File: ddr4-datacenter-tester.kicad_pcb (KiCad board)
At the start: 8 copper layers, 152.9 x 90 mm, 377 parts, among them IC1 TPS54561, IC3 TPD8S009DSMR, J1 0878311420, J10 61300311121, J3 DC_SOCKET, J4 WE_629105150521, J5 2309409-1, J6 685119134923, J7 1140084168, J8 61300311121, Q2 BSS138APW, Q3 BSS138APW, Q4 BSS138APW, Q5 BSS138APW, Q6 BSS138APW, Q7 BSS138APW, Q8 BSS138APW, U1 XC7K70T-FBG484, U10 LM3881MME_NOPB, U11 S27KL0641DABHI023, U12 TPS62823DLCT, U13 XC7K160T-2FFG676C, U14 2199155-1, U2 ASFLMB-100.000MHZ-XY-T, U3 S25FL128SAGNFI000, U4 TPS65296, U5 TPS62823DLCT, U6 KSZ9031RNXCA, U7 FT4232HQ, U8 SRST, U9 TPS62823DLCT, Y1 ABM8G-25.000MHZ-18-D2Y-T, Y2 ABM8G-12.000MHZ-18-D2Y-T

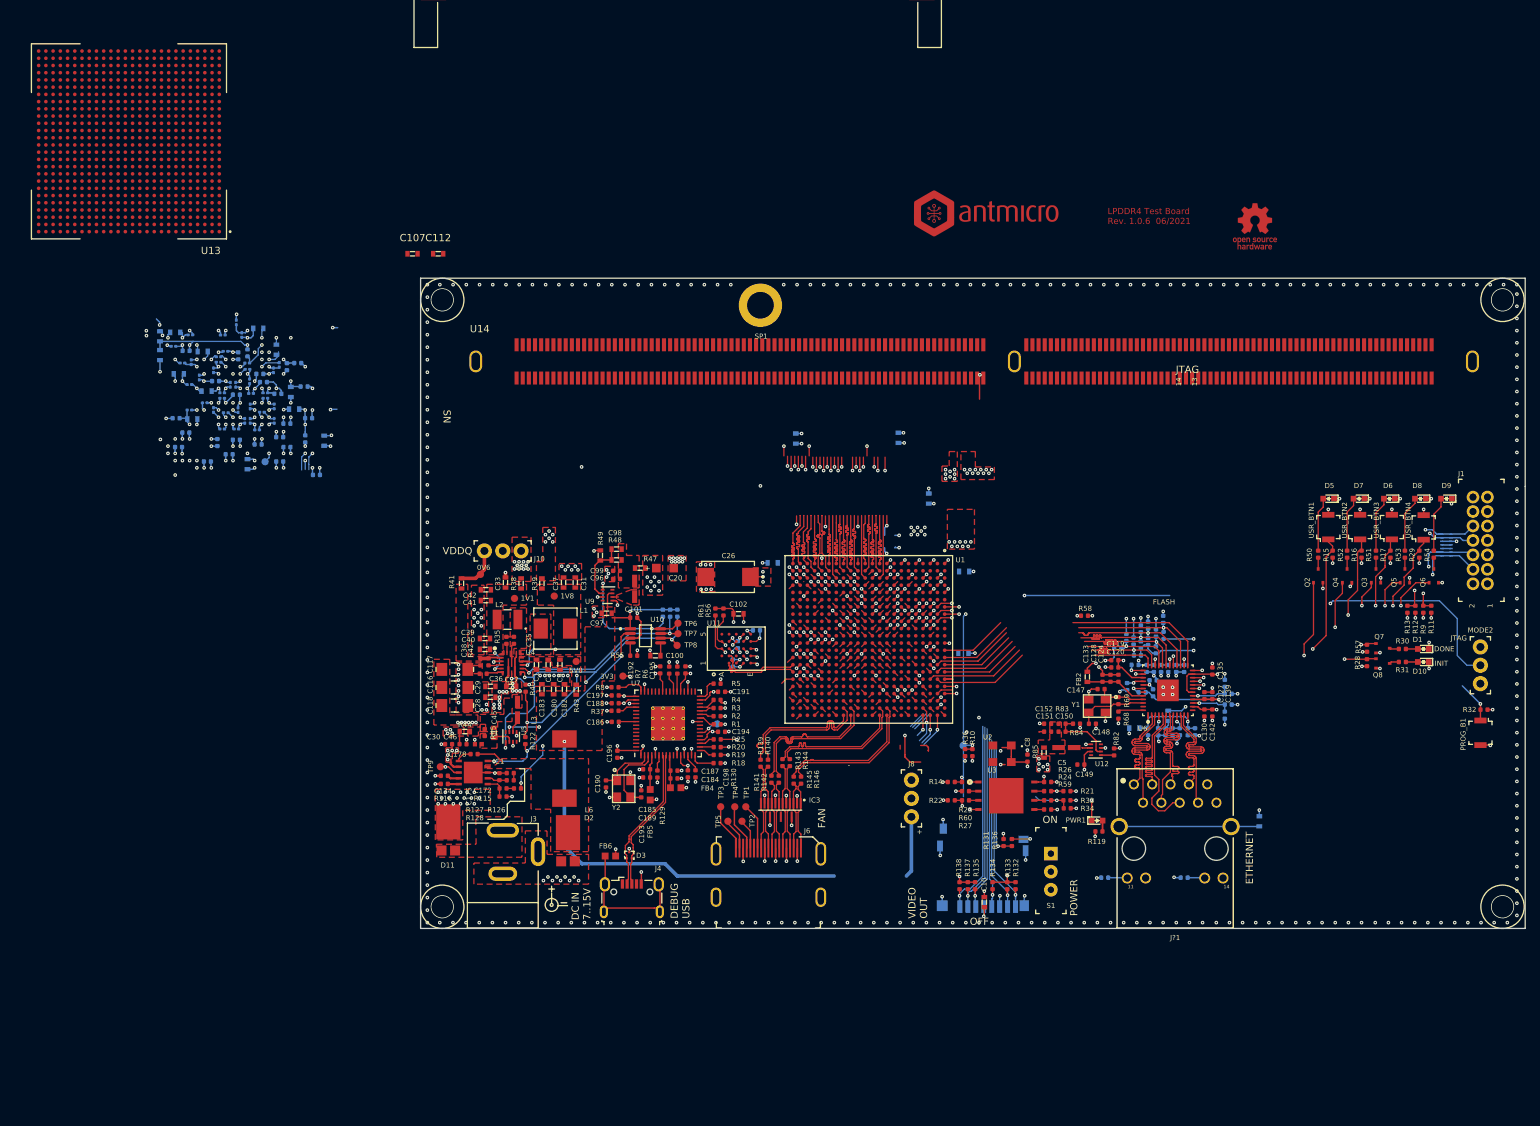
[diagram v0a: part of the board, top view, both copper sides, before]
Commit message: Component placement draft
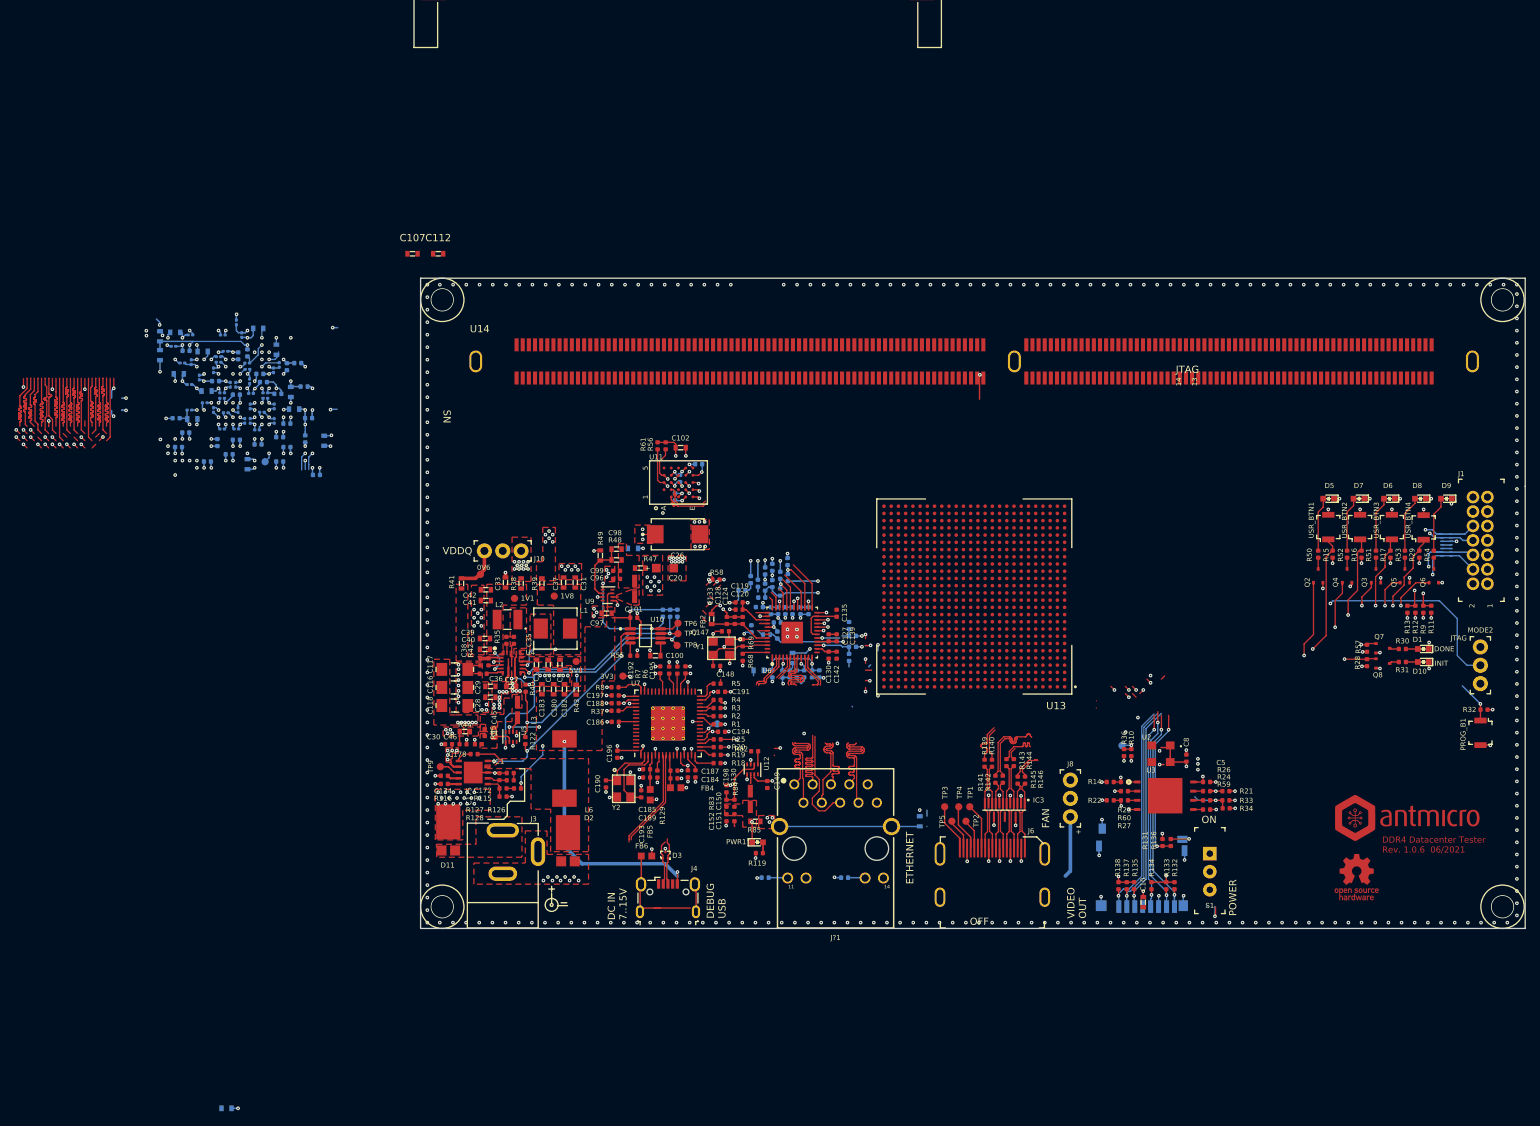
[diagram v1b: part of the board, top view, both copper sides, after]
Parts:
- removed C106, C108, C110, C111: C_10n_0603, ddr4-datacenter-tester-footprints:0603-cap
- removed SP1: 9774050151, ddr4-datacenter-tester-footprints:9774050151
- removed U1: XC7K70T-FBG484, ddr4-datacenter-tester-footprints:BGA484C100P22X22_2300X2300X244N
- moved U13 132.9 mm to (183.6, 90.1)
- moved C113 119.9 mm to (80.1, 160.9)
- moved N2 102.0 mm to (243.6, 120.9)
- moved N1 91.2 mm to (236.6, 128.9)
- moved C119 52.6 mm to (151.1, 90.9)
- moved C120 52.6 mm to (151.1, 91.9)
- moved C121 52.6 mm to (157.1, 100.8)
- moved C122 52.6 mm to (157.5, 92.0)
- moved C123 52.6 mm to (155.5, 92.0)
- moved C124 52.6 mm to (151.6, 93.4)
- moved C125 52.6 mm to (160.1, 100.8)
- moved C126 52.6 mm to (159.6, 92.0)
- moved C127 52.6 mm to (163.5, 95.8)
- moved C128 52.6 mm to (150.5, 93.4)
- moved C129 52.6 mm to (158.1, 100.8)
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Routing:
- net GND: track 317.8 -> 237.5 mm, vias 516 -> 465
- net TCK_JTAG: track 97.1 -> 31.1 mm
- net TDO_JTAG: track 94.5 -> 29.6 mm
- net TDI_JTAG: track 96.3 -> 31.9 mm
- net TMS_JTAG: track 91.1 -> 26.8 mm
- net /Supply/SYS_EN: track 85.0 -> 22.4 mm, vias 1 -> 0
- net /Supply/VCC_IO_EN: track 137.1 -> 84.7 mm, vias 5 -> 4
- net PROGRAM_B: track 53.2 -> 5.91 mm, vias 3 -> 1
- net DONE: track 41.4 -> 5.33 mm, vias 2 -> 1
- net CCLK: track 41.1 -> 5.95 mm, vias 3 -> 1
- net INIT_B: track 35.1 -> 5.05 mm, vias 2 -> 1
- net 3V3_SYS: track 156.3 -> 126.3 mm, vias 87 -> 86
- net MODE0: track 42.3 -> 13.0 mm, vias 2 -> 1
- net MODE1: track 41.2 -> 12.0 mm, vias 2 -> 1
- net ETH_RXD0: track 32.2 -> 5.04 mm
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- removed copper zone on F.Cu, net VDDQ
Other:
- board text added: "DDR4 Datacenter Tester Rev. 1.0.0 06/2021"
- board text added: "DDR4 Datacenter Tester Rev. 1.0.6 06/2021"
- board text removed: "-"
- board text removed: "FLASH"
- board text removed: "LPDDR4 Test Board Rev. 1.0.6 06/2021"

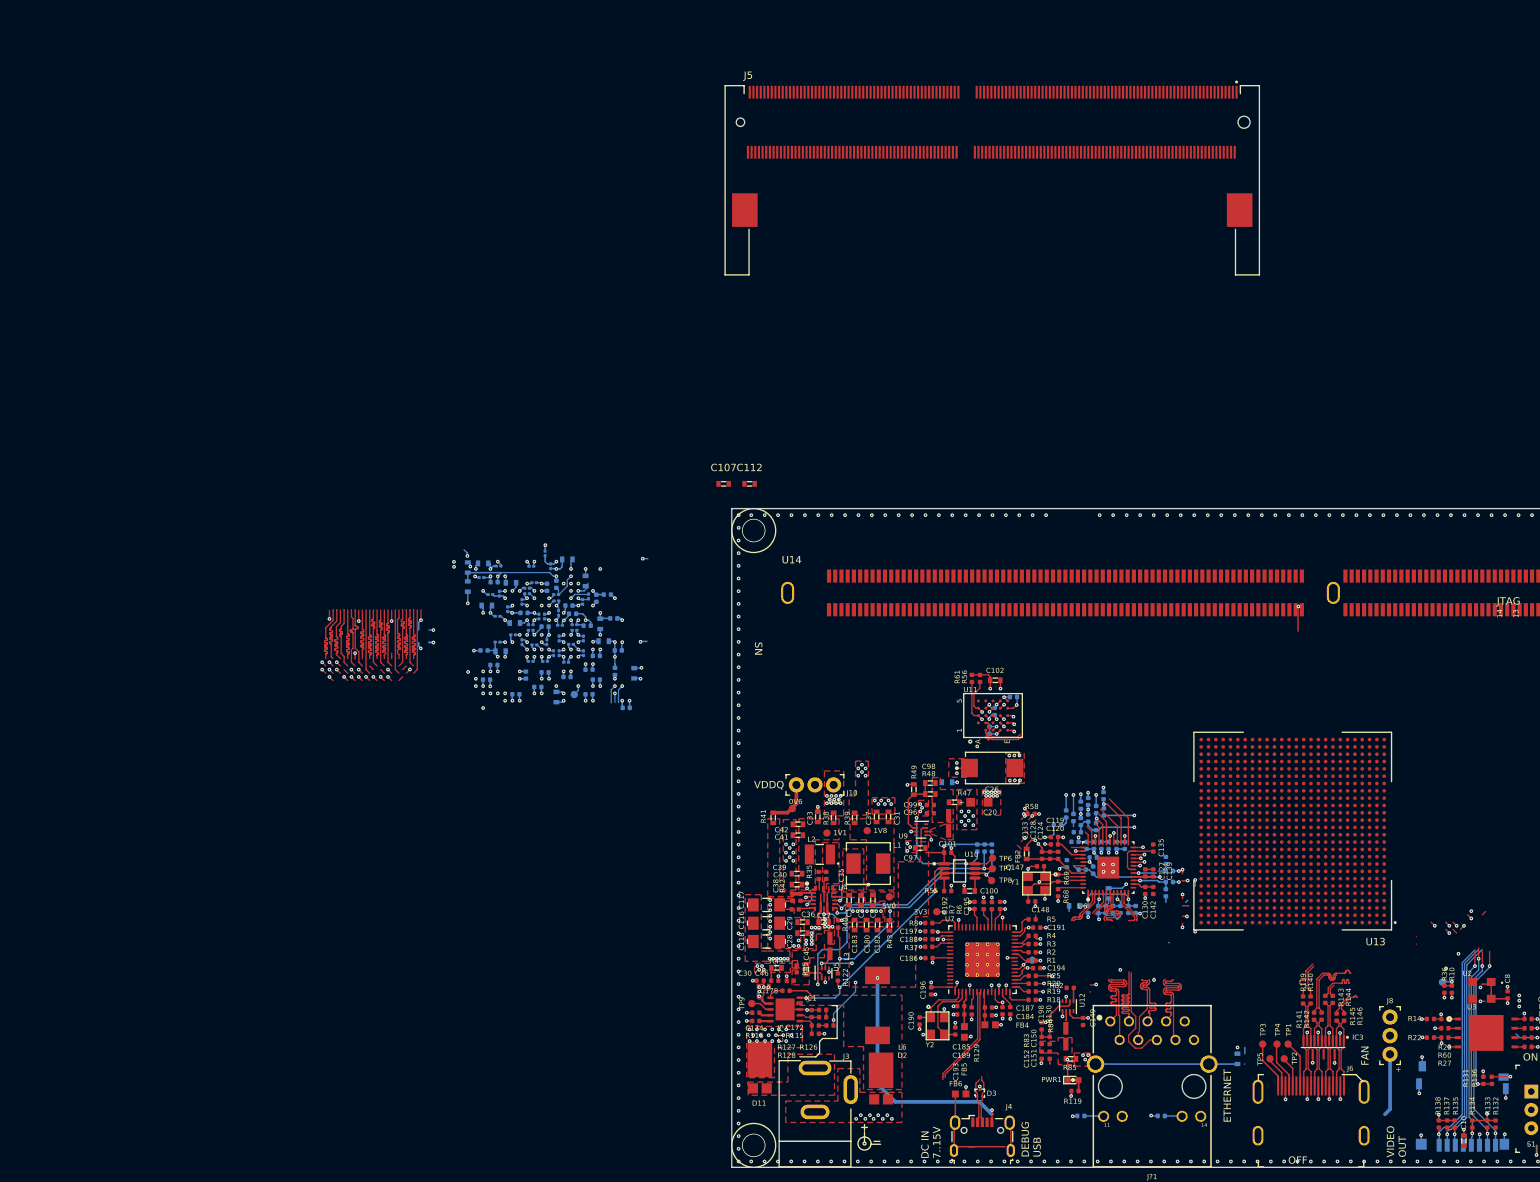
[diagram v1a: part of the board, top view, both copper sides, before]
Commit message: Add DD4 pinout, connect ethernet, QSPI, TMDS, SDIO
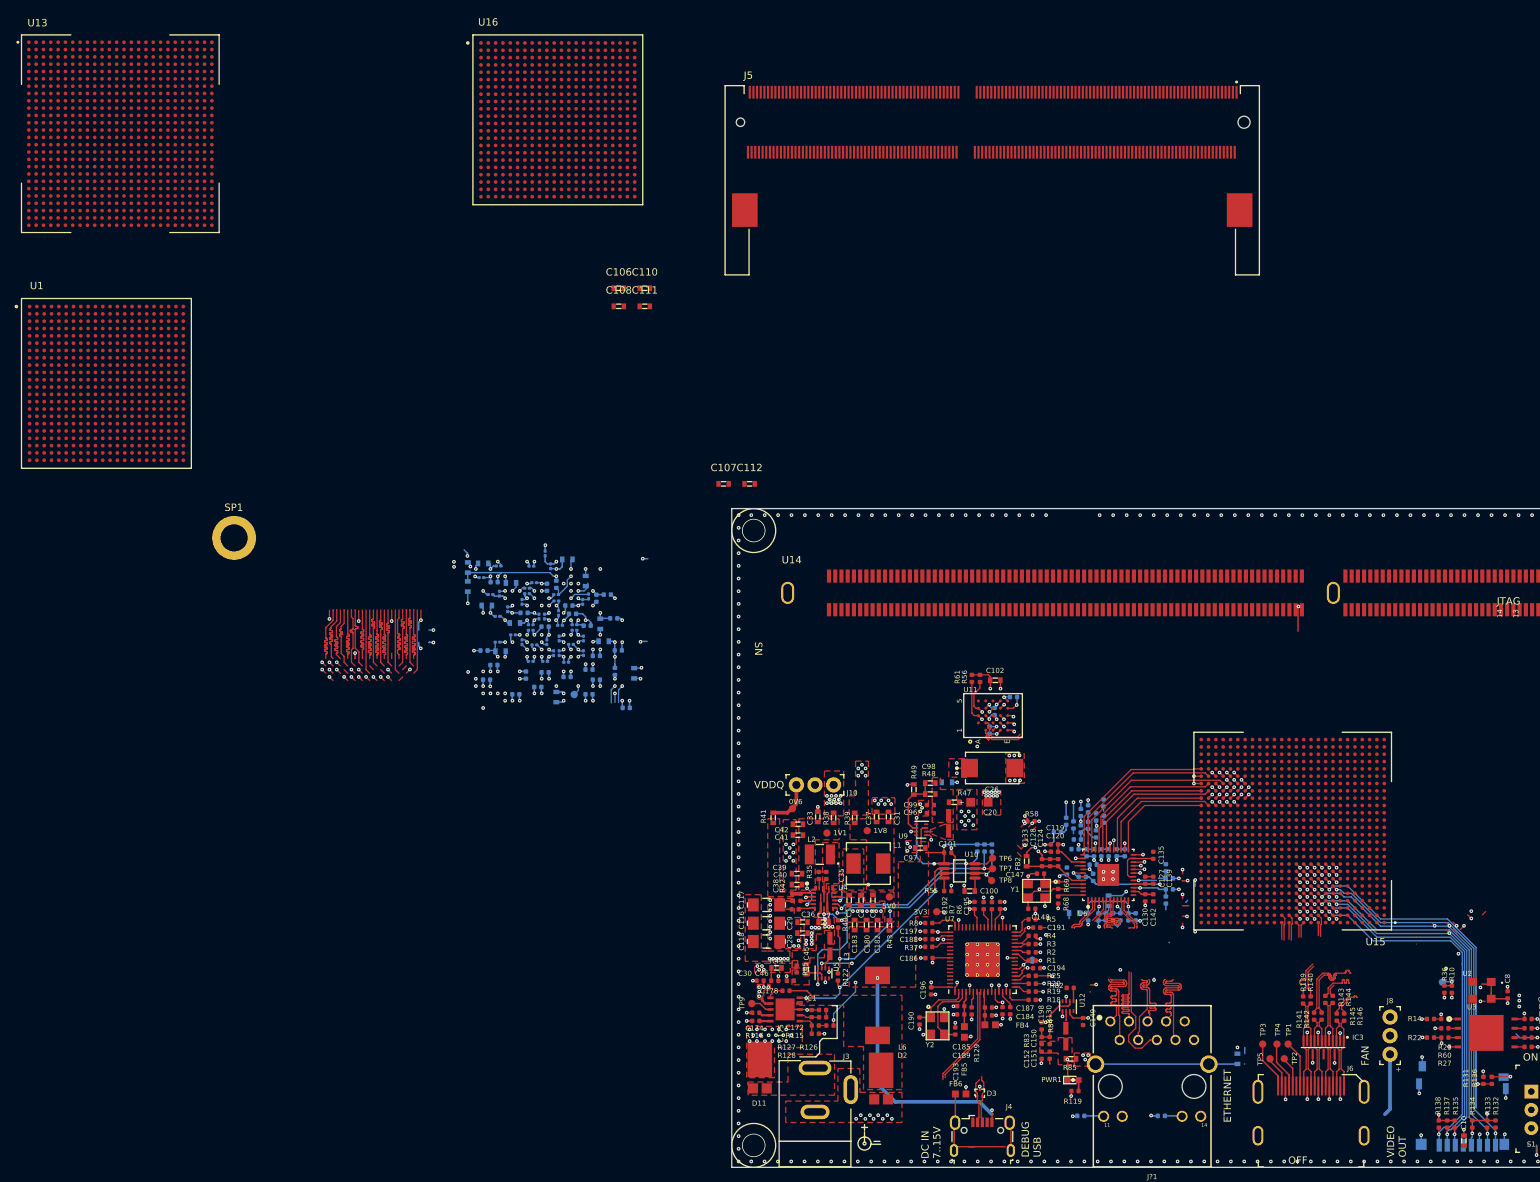
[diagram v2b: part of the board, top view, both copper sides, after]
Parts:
- added C106: C_10n_0603, ddr4-datacenter-tester-footprints:0603-cap, F.Cu at (91.6, 15.9)
- added C108: C_10n_0603, ddr4-datacenter-tester-footprints:0603-cap, F.Cu at (91.6, 18.4)
- added C110: C_10n_0603, ddr4-datacenter-tester-footprints:0603-cap, F.Cu at (95.1, 15.9)
- added C111: C_10n_0603, ddr4-datacenter-tester-footprints:0603-cap, F.Cu at (95.1, 18.4)
- added SP1: 9774050151, ddr4-datacenter-tester-footprints:9774050151, F.Cu at (39.0, 50.1)
- added U1: XC7K70T-FBG484, ddr4-datacenter-tester-footprints:BGA484C100P22X22_2300X2300X244N, F.Cu at (21.6, 28.9)
- added U15: XC7K160T-FFG676, antmicro-footprints:BGA676C100P26X26_2700X2700X254, F.Cu at (183.6, 90.1)
- added U16: XC7K70T-FBG484, ddr4-datacenter-tester-footprints:BGA484C100P22X22_2300X2300X244N, F.Cu at (83.2, -7.11)
- moved U13 186.4 mm to (23.5, -5.21), turned to 0 degrees
- moved C119 1.00 mm to (151.1, 91.9)
- moved C120 1.00 mm to (151.1, 92.9)
- moved C121 1.00 mm to (157.1, 101.8)
- moved C122 1.00 mm to (157.5, 93.0)
- moved C123 1.00 mm to (155.5, 93.0)
- moved C124 1.00 mm to (151.6, 94.4)
- moved C125 1.00 mm to (160.1, 101.8)
- moved C126 1.00 mm to (159.6, 93.0)
- moved C127 1.00 mm to (163.5, 96.8)
- moved C128 1.00 mm to (150.5, 94.4)
- moved C129 1.00 mm to (158.1, 101.8)
- moved C130 1.00 mm to (163.5, 99.2)
- moved C131 1.00 mm to (156.5, 93.0)
- moved C132 1.00 mm to (155.7, 101.8)
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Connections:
- net Net-(U14-Pad10) renamed /DDR4/DQ6
- net Net-(U14-Pad100) renamed /DDR4/DQS13_C
- net Net-(U14-Pad102) renamed /DDR4/DQ38
- net Net-(U14-Pad104) renamed /DDR4/DQ34
- net Net-(U14-Pad106) renamed /DDR4/DQ44
- net Net-(U14-Pad108) renamed /DDR4/DQ40
- net Net-(U14-Pad110) renamed /DDR4/DQS14_T
- net Net-(U14-Pad111) renamed /DDR4/DQS14_C
- net Net-(U14-Pad113) renamed /DDR4/DQ46
- net Net-(U14-Pad115) renamed /DDR4/DQ42
- net Net-(U14-Pad117) renamed /DDR4/DQ52
- net Net-(U14-Pad119) renamed /DDR4/DQ48
- net Net-(U14-Pad12) renamed /DDR4/DQ2
- net Net-(U14-Pad121) renamed /DDR4/DQS15_T
- net Net-(U14-Pad122) renamed /DDR4/DQS15_C
- net Net-(U14-Pad124) renamed /DDR4/DQ54
- net Net-(U14-Pad126) renamed /DDR4/DQ50
- net Net-(U14-Pad128) renamed /DDR4/DQ60
- net Net-(U14-Pad130) renamed /DDR4/DQ56
- net Net-(U14-Pad132) renamed /DDR4/DQS16_T
- net Net-(U14-Pad133) renamed /DDR4/DQS16_C
- net Net-(U14-Pad135) renamed /DDR4/DQ62
- net Net-(U14-Pad137) renamed /DDR4/DQ58
- net Net-(U14-Pad139) renamed /DDR4/SA0
- net Net-(U14-Pad14) renamed /DDR4/DQ12
- net Net-(U14-Pad140) renamed /DDR4/SA1
- net Net-(U14-Pad141) renamed /DDR4/SCL
- net Net-(U14-Pad146) renamed VREFCA
- net Net-(U14-Pad148) renamed /DDR4/DQ5
- net Net-(U14-Pad150) renamed /DDR4/DQ1
- net Net-(U14-Pad155) renamed /DDR4/DQ7
- net Net-(U14-Pad157) renamed /DDR4/DQ3
- net Net-(U14-Pad159) renamed /DDR4/DQ13
- net Net-(U14-Pad16) renamed /DDR4/DQ8
- net Net-(U14-Pad161) renamed /DDR4/DQ9
- net Net-(U14-Pad163) renamed /DDR4/DQS1_C
- net Net-(U14-Pad164) renamed /DDR4/DQS1_T
- net Net-(U14-Pad166) renamed /DDR4/DQ15
- net Net-(U14-Pad168) renamed /DDR4/DQ11
- net Net-(U14-Pad170) renamed /DDR4/DQ21
- net Net-(U14-Pad172) renamed /DDR4/DQ17
- net Net-(U14-Pad174) renamed /DDR4/DQS2_C
- net Net-(U14-Pad175) renamed /DDR4/DQS2_T
- net Net-(U14-Pad177) renamed /DDR4/DQ23
- net Net-(U14-Pad179) renamed /DDR4/DQ19
- net Net-(U14-Pad181) renamed /DDR4/DQ29
- net Net-(U14-Pad183) renamed /DDR4/DQ25
- net Net-(U14-Pad185) renamed /DDR4/DQS3_C
- net Net-(U14-Pad186) renamed /DDR4/DQS3_T
- net Net-(U14-Pad188) renamed /DDR4/DQ31
- net Net-(U14-Pad190) renamed /DDR4/DQ27
- net Net-(U14-Pad192) renamed /DDR4/CB5
- net Net-(U14-Pad194) renamed /DDR4/CB1
- net Net-(U14-Pad196) renamed /DDR4/DQS8_C
- net Net-(U14-Pad197) renamed /DDR4/DQS8_T
- net Net-(U14-Pad199) renamed /DDR4/CB7
- net Net-(U14-Pad201) renamed /DDR4/CB3
- net Net-(U14-Pad203) renamed /DDR4/CKE1\NC
- net Net-(U14-Pad207) renamed /DDR4/BG1
- net Net-(U14-Pad208) renamed /DDR4/~ALERT
- net Net-(U14-Pad21) renamed /DDR4/DQ14
- net Net-(U14-Pad210) renamed /DDR4/A11
- net Net-(U14-Pad211) renamed /DDR4/A7
- net Net-(U14-Pad213) renamed /DDR4/A5
- net Net-(U14-Pad214) renamed /DDR4/A4
- net Net-(U14-Pad216) renamed /DDR4/A2
- net Net-(U14-Pad218) renamed /DDR4/CK1_T
- net Net-(U14-Pad219) renamed /DDR4/CK1_C
- net Net-(U14-Pad222) renamed /DDR4/PARITY
- net Net-(U14-Pad224) renamed /DDR4/BA1
- net Net-(U14-Pad225) renamed /DDR4/A10\AP
- net Net-(U14-Pad228) renamed /DDR4/~WE~\A14
- net Net-(U14-Pad23) renamed /DDR4/DQ10
- net Net-(U14-Pad230) renamed /DDR4/~SAVE
- net Net-(U14-Pad232) renamed /DDR4/A13
- net Net-(U14-Pad234) renamed /DDR4/A17
- net Net-(U14-Pad235) renamed /DDR4/NC\C2
- net Net-(U14-Pad237) renamed /DDR4/~CS3~\C1,NC
- net Net-(U14-Pad238) renamed /DDR4/SA2
- net Net-(U14-Pad240) renamed /DDR4/DQ37
- net Net-(U14-Pad242) renamed /DDR4/DQ33
- net Net-(U14-Pad244) renamed /DDR4/DQS4_C
- net Net-(U14-Pad245) renamed /DDR4/DQS4_T
- net Net-(U14-Pad247) renamed /DDR4/DQ39
- net Net-(U14-Pad249) renamed /DDR4/DQ35
- net Net-(U14-Pad25) renamed /DDR4/DQ20
- net Net-(U14-Pad251) renamed /DDR4/DQ45
- net Net-(U14-Pad253) renamed /DDR4/DQ41
- net Net-(U14-Pad255) renamed /DDR4/DQS5_C
- net Net-(U14-Pad256) renamed /DDR4/DQS5_T
- net Net-(U14-Pad258) renamed /DDR4/DQ47
- net Net-(U14-Pad260) renamed /DDR4/DQ43
- net Net-(U14-Pad262) renamed /DDR4/DQ53
- net Net-(U14-Pad264) renamed /DDR4/DQ49
- net Net-(U14-Pad266) renamed /DDR4/DQS6_C
- net Net-(U14-Pad267) renamed /DDR4/DQS6_T
- net Net-(U14-Pad269) renamed /DDR4/DQ55
- net Net-(U14-Pad27) renamed /DDR4/DQ16
- net Net-(U14-Pad271) renamed /DDR4/DQ51
- net Net-(U14-Pad273) renamed /DDR4/DQ61
- net Net-(U14-Pad275) renamed /DDR4/DQ57
- net Net-(U14-Pad277) renamed /DDR4/DQS7_C
- net Net-(U14-Pad278) renamed /DDR4/DQS7_T
- net Net-(U14-Pad280) renamed /DDR4/DQ63
- net Net-(U14-Pad282) renamed /DDR4/DQ59
- net Net-(U14-Pad284) renamed VDDSPD
- net Net-(U14-Pad285) renamed /DDR4/SDA
- net Net-(U14-Pad29) renamed /DDR4/DQS11_T
- net Net-(U14-Pad3) renamed /DDR4/DQ4
- net Net-(U14-Pad30) renamed /DDR4/DQS11_C
- net Net-(U14-Pad32) renamed /DDR4/DQ22
- net Net-(U14-Pad34) renamed /DDR4/DQ18
- net Net-(U14-Pad36) renamed /DDR4/DQ28
- net Net-(U14-Pad38) renamed /DDR4/DQ24
- net Net-(U14-Pad40) renamed /DDR4/DQS12_T
- net Net-(U14-Pad41) renamed /DDR4/DQS12_C
- net Net-(U14-Pad43) renamed /DDR4/DQ30
- net Net-(U14-Pad45) renamed /DDR4/DQ26
- net Net-(U14-Pad47) renamed /DDR4/CB4
- net Net-(U14-Pad49) renamed /DDR4/CB0
- net Net-(U14-Pad5) renamed /DDR4/DQ0
- net Net-(U14-Pad51) renamed /DDR4/DQS17_T
- net Net-(U14-Pad52) renamed /DDR4/DQS17_C
- net Net-(U14-Pad54) renamed /DDR4/CB6
- net Net-(U14-Pad56) renamed /DDR4/CB2
- net Net-(U14-Pad58) renamed /DDR4/~RESET
- net Net-(U14-Pad60) renamed /DDR4/CKE0
- net Net-(U14-Pad62) renamed /DDR4/~ACT
- net Net-(U14-Pad63) renamed /DDR4/BG0
- net Net-(U14-Pad65) renamed /DDR4/A12\~BC
- net Net-(U14-Pad66) renamed /DDR4/A9
- net Net-(U14-Pad68) renamed /DDR4/A8
- net Net-(U14-Pad69) renamed /DDR4/A6
- net Net-(U14-Pad7) renamed /DDR4/DQS9_T
- net Net-(U14-Pad71) renamed /DDR4/A3
- net Net-(U14-Pad72) renamed /DDR4/A1
- net Net-(U14-Pad74) renamed /DDR4/CK0_T
- net Net-(U14-Pad75) renamed /DDR4/CK0_C
- net Net-(U14-Pad78) renamed /DDR4/~EVENT
- net Net-(U14-Pad79) renamed /DDR4/A0
- net Net-(U14-Pad8) renamed /DDR4/DQS9_C
- net Net-(U14-Pad81) renamed /DDR4/BA0
- net Net-(U14-Pad82) renamed /DDR4/~RAS~\A16
- net Net-(U14-Pad84) renamed /DDR4/~CS0
- net Net-(U14-Pad86) renamed /DDR4/~CAS~\A15
- net Net-(U14-Pad87) renamed /DDR4/ODT0
- net Net-(U14-Pad89) renamed /DDR4/~CS1~\NC
- net Net-(U14-Pad91) renamed /DDR4/ODT1\NC
- net Net-(U14-Pad93) renamed /DDR4/~CS2~\C0
- net Net-(U14-Pad95) renamed /DDR4/DQ36
- net Net-(U14-Pad97) renamed /DDR4/DQ32
- net Net-(U14-Pad99) renamed /DDR4/DQS13_T
- U14 pad 1: Net-(U14-Pad1) -> /DDR4/12V
- U14 pad 101: Net-(U14-Pad101) -> VSS
- U14 pad 103: Net-(U14-Pad103) -> VSS
- U14 pad 105: Net-(U14-Pad105) -> VSS
- U14 pad 107: Net-(U14-Pad107) -> VSS
- U14 pad 109: Net-(U14-Pad109) -> VSS
- U14 pad 11: Net-(U14-Pad11) -> VSS
- U14 pad 112: Net-(U14-Pad112) -> VSS
- U14 pad 114: Net-(U14-Pad114) -> VSS
- U14 pad 116: Net-(U14-Pad116) -> VSS
- U14 pad 118: Net-(U14-Pad118) -> VSS
- U14 pad 120: Net-(U14-Pad120) -> VSS
- U14 pad 123: Net-(U14-Pad123) -> VSS
- U14 pad 125: Net-(U14-Pad125) -> VSS
- U14 pad 127: Net-(U14-Pad127) -> VSS
- U14 pad 129: Net-(U14-Pad129) -> VSS
- U14 pad 13: Net-(U14-Pad13) -> VSS
- U14 pad 131: Net-(U14-Pad131) -> VSS
- U14 pad 134: Net-(U14-Pad134) -> VSS
- U14 pad 136: Net-(U14-Pad136) -> VSS
- U14 pad 138: Net-(U14-Pad138) -> VSS
- U14 pad 142: Net-(U14-Pad142) -> VPP
- U14 pad 143: Net-(U14-Pad143) -> VPP
- U14 pad 145: Net-(U14-Pad145) -> /DDR4/12V
- U14 pad 147: Net-(U14-Pad147) -> VSS
- U14 pad 149: Net-(U14-Pad149) -> VSS
- U14 pad 15: Net-(U14-Pad15) -> VSS
- U14 pad 151: Net-(U14-Pad151) -> VSS
- U14 pad 152: Net-(U14-Pad152) -> /DDR4/DQS10_C
- U14 pad 153: Net-(U14-Pad153) -> /DDR4/DQS10_T
- U14 pad 154: Net-(U14-Pad154) -> VSS
- U14 pad 156: Net-(U14-Pad156) -> VSS
- U14 pad 158: Net-(U14-Pad158) -> VSS
- U14 pad 160: Net-(U14-Pad160) -> VSS
- U14 pad 162: Net-(U14-Pad162) -> VSS
- U14 pad 165: Net-(U14-Pad165) -> VSS
- U14 pad 167: Net-(U14-Pad167) -> VSS
- U14 pad 169: Net-(U14-Pad169) -> VSS
- U14 pad 17: Net-(U14-Pad17) -> VSS
- U14 pad 171: Net-(U14-Pad171) -> VSS
- U14 pad 173: Net-(U14-Pad173) -> VSS
- U14 pad 176: Net-(U14-Pad176) -> VSS
- U14 pad 178: Net-(U14-Pad178) -> VSS
- U14 pad 18: Net-(U14-Pad18) -> /DDR4/DQS10_T
- U14 pad 180: Net-(U14-Pad180) -> VSS
- U14 pad 182: Net-(U14-Pad182) -> VSS
- U14 pad 184: Net-(U14-Pad184) -> VSS
- U14 pad 187: Net-(U14-Pad187) -> VSS
- U14 pad 189: Net-(U14-Pad189) -> VSS
- U14 pad 19: Net-(U14-Pad19) -> /DDR4/DQS10_C
- U14 pad 191: Net-(U14-Pad191) -> VSS
- U14 pad 193: Net-(U14-Pad193) -> VSS
- U14 pad 195: Net-(U14-Pad195) -> VSS
- U14 pad 198: Net-(U14-Pad198) -> VSS
- U14 pad 2: Net-(U14-Pad2) -> VSS
- U14 pad 20: Net-(U14-Pad20) -> VSS
- U14 pad 200: Net-(U14-Pad200) -> VSS
- U14 pad 202: Net-(U14-Pad202) -> VSS
- U14 pad 204: Net-(U14-Pad204) -> VSS
- U14 pad 206: Net-(U14-Pad206) -> VSS
- U14 pad 209: Net-(U14-Pad209) -> VSS
- U14 pad 212: Net-(U14-Pad212) -> VSS
- U14 pad 215: Net-(U14-Pad215) -> VSS
- U14 pad 217: Net-(U14-Pad217) -> VSS
- U14 pad 22: Net-(U14-Pad22) -> VSS
- U14 pad 220: Net-(U14-Pad220) -> VSS
- U14 pad 221: Net-(U14-Pad221) -> VTT
- U14 pad 223: Net-(U14-Pad223) -> VDD
- U14 pad 226: Net-(U14-Pad226) -> VDD
- U14 pad 229: Net-(U14-Pad229) -> VDD
- U14 pad 231: Net-(U14-Pad231) -> VDD
- U14 pad 233: Net-(U14-Pad233) -> VDD
- U14 pad 236: Net-(U14-Pad236) -> VDD
- U14 pad 239: Net-(U14-Pad239) -> VSS
- U14 pad 24: Net-(U14-Pad24) -> VSS
- U14 pad 241: Net-(U14-Pad241) -> VSS
- U14 pad 243: Net-(U14-Pad243) -> VSS
- U14 pad 246: Net-(U14-Pad246) -> VSS
- U14 pad 248: Net-(U14-Pad248) -> VSS
- U14 pad 250: Net-(U14-Pad250) -> VSS
- U14 pad 252: Net-(U14-Pad252) -> VSS
- U14 pad 254: Net-(U14-Pad254) -> VSS
- U14 pad 257: Net-(U14-Pad257) -> VSS
- U14 pad 259: Net-(U14-Pad259) -> VSS
- U14 pad 26: Net-(U14-Pad26) -> VSS
- U14 pad 261: Net-(U14-Pad261) -> VSS
- U14 pad 263: Net-(U14-Pad263) -> VSS
- U14 pad 265: Net-(U14-Pad265) -> VSS
- U14 pad 268: Net-(U14-Pad268) -> VSS
- U14 pad 270: Net-(U14-Pad270) -> VSS
- U14 pad 272: Net-(U14-Pad272) -> VSS
- U14 pad 274: Net-(U14-Pad274) -> VSS
- U14 pad 276: Net-(U14-Pad276) -> VSS
- U14 pad 279: Net-(U14-Pad279) -> VSS
- U14 pad 28: Net-(U14-Pad28) -> VSS
- U14 pad 281: Net-(U14-Pad281) -> VSS
- U14 pad 283: Net-(U14-Pad283) -> VSS
- U14 pad 286: Net-(U14-Pad286) -> VPP
- U14 pad 287: Net-(U14-Pad287) -> VPP
- U14 pad 288: Net-(U14-Pad288) -> VPP
- U14 pad 31: Net-(U14-Pad31) -> VSS
- U14 pad 33: Net-(U14-Pad33) -> VSS
- U14 pad 35: Net-(U14-Pad35) -> VSS
- U14 pad 37: Net-(U14-Pad37) -> VSS
- U14 pad 39: Net-(U14-Pad39) -> VSS
- U14 pad 4: Net-(U14-Pad4) -> VSS
- U14 pad 42: Net-(U14-Pad42) -> VSS
- U14 pad 44: Net-(U14-Pad44) -> VSS
- U14 pad 46: Net-(U14-Pad46) -> VSS
- U14 pad 48: Net-(U14-Pad48) -> VSS
- U14 pad 50: Net-(U14-Pad50) -> VSS
- U14 pad 53: Net-(U14-Pad53) -> VSS
- U14 pad 55: Net-(U14-Pad55) -> VSS
- U14 pad 57: Net-(U14-Pad57) -> VSS
- U14 pad 59: Net-(U14-Pad59) -> VDD
- U14 pad 6: Net-(U14-Pad6) -> VSS
- U14 pad 61: Net-(U14-Pad61) -> VDD
- U14 pad 64: Net-(U14-Pad64) -> VDD
- U14 pad 67: Net-(U14-Pad67) -> VDD
- U14 pad 70: Net-(U14-Pad70) -> VDD
- U14 pad 73: Net-(U14-Pad73) -> VDD
- U14 pad 76: Net-(U14-Pad76) -> VDD
- U14 pad 77: Net-(U14-Pad77) -> VTT
- U14 pad 80: Net-(U14-Pad80) -> VDD
- U14 pad 83: Net-(U14-Pad83) -> VDD
- U14 pad 85: Net-(U14-Pad85) -> VDD
- U14 pad 88: Net-(U14-Pad88) -> VDD
- U14 pad 9: Net-(U14-Pad9) -> VSS
- U14 pad 90: Net-(U14-Pad90) -> VDD
- U14 pad 92: Net-(U14-Pad92) -> VDD
- U14 pad 94: Net-(U14-Pad94) -> VSS
- U14 pad 96: Net-(U14-Pad96) -> VSS
- U14 pad 98: Net-(U14-Pad98) -> VSS
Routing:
- net SD_CD: track 21.0 -> 78.9 mm
- net ETH_INT_N: track 1.00 -> 34.3 mm, vias 1 -> 2
- net ETH_RSTN: track 2.24 -> 34.2 mm, vias 1 -> 3
- net ETH_REF_CLK: track 4.18 -> 31.0 mm, vias 1 -> 2
- net SD_DAT0: track 29.4 -> 53.3 mm
- net SD_CLK: track 27.8 -> 51.6 mm
- net SD_DAT1: track 29.5 -> 52.2 mm
- net ETH_MDIO: track 8.87 -> 31.4 mm
- net ETH_TXD3: track 7.53 -> 30.0 mm, vias 1 -> 2
- net ETH_MDC: track 1.61 -> 23.7 mm
- net ETH_RX_CLK: track 3.78 -> 25.8 mm
- net ETH_TXD2: track 25.2 -> 46.4 mm, vias 2 -> 3
- net SD_DAT3: track 30.8 -> 51.6 mm, vias 2 -> 3
- net SD_DAT2: track 32.6 -> 52.9 mm, vias 2 -> 3
- net SD_CMD: track 31.7 -> 51.8 mm, vias 2 -> 3
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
